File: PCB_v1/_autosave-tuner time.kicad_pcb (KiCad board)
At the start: 2 copper layers, 121 parts, among them J3 Conn_01x05_Pin, J4 Conn_01x05_Pin, J5 OLED Module Mount, SW7 SW_Push, SW8 SW_Push, U2 BQ27441-G1

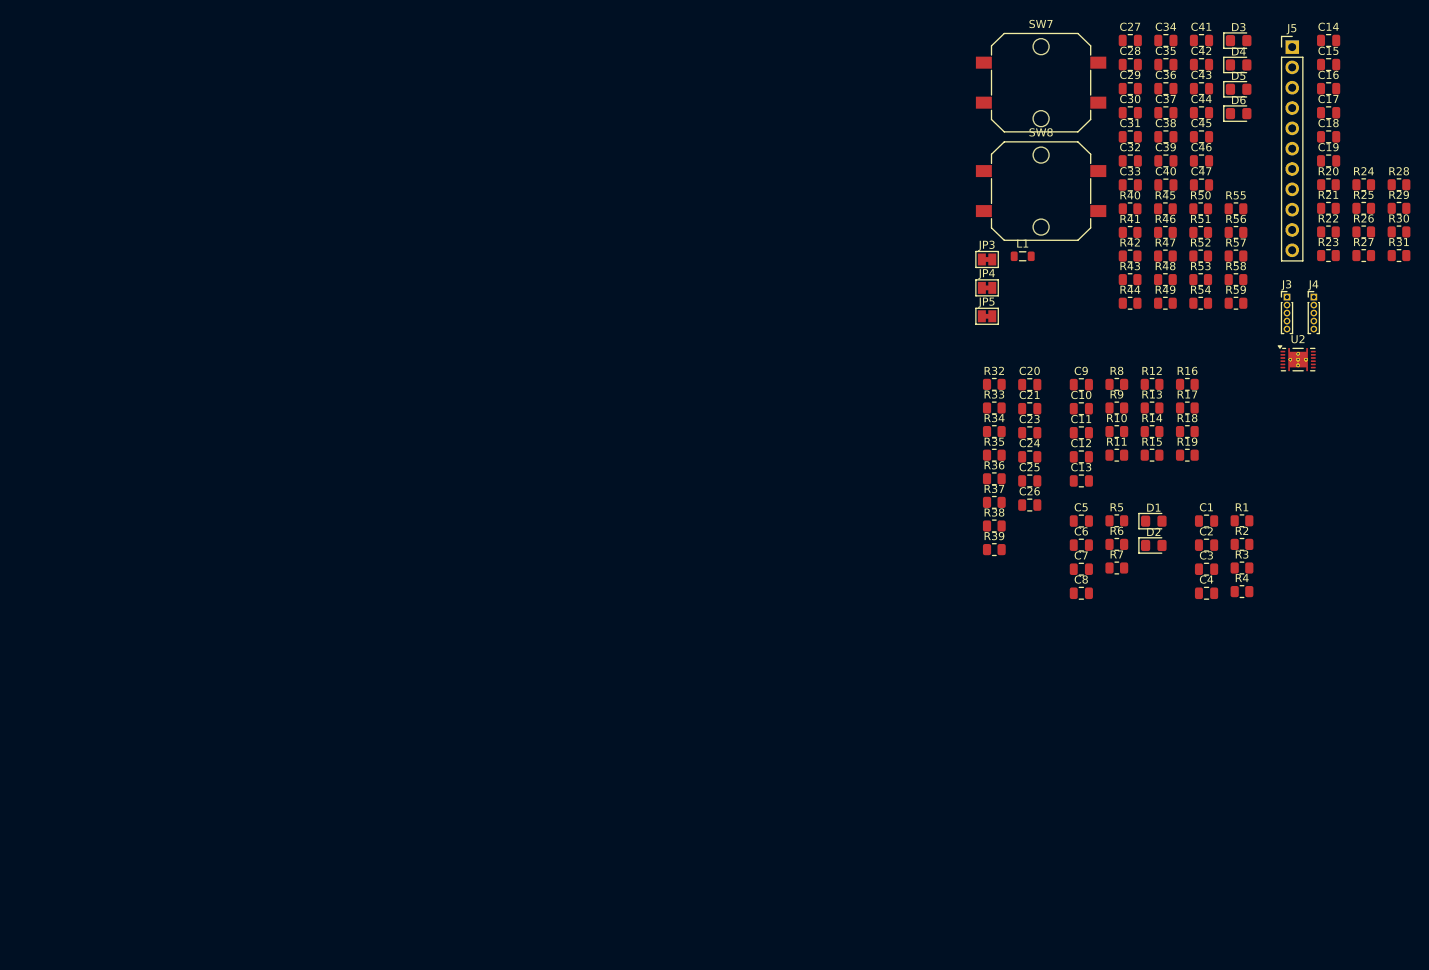
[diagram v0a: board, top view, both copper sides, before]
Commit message: adding the parts library
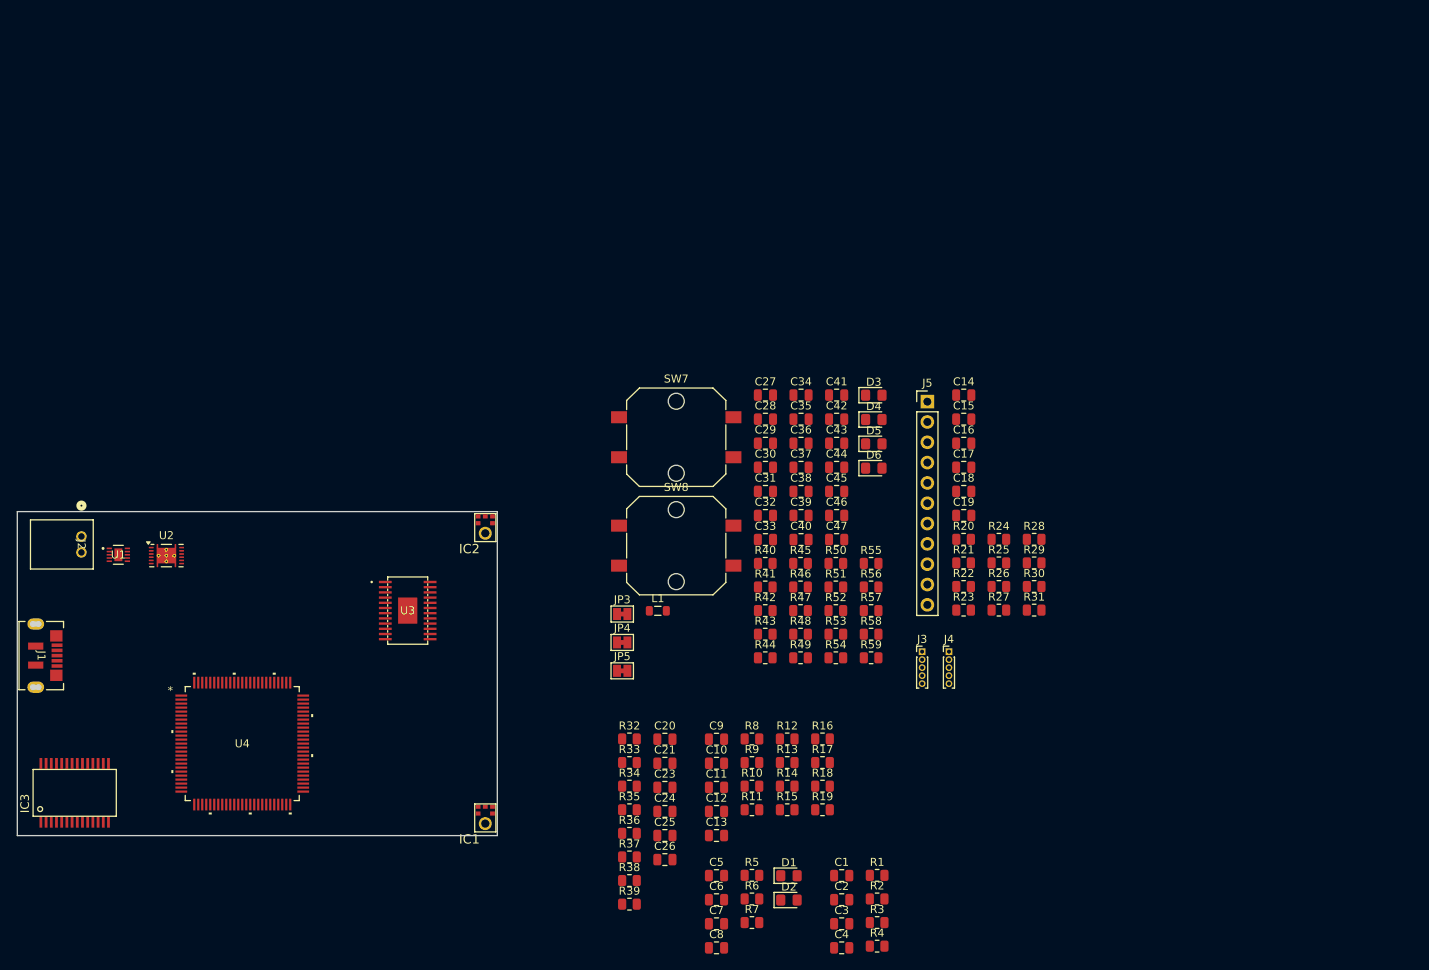
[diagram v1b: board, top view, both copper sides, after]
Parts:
- added IC1: MIC_I2S_SPH0645, Parts_Library:SPH0645LM4H, F.Cu at (153.5, 133.3)
- added IC2: MIC_I2S_SPH0645, Parts_Library:SPH0645LM4H, F.Cu at (153.5, 97.0)
- added IC3: FT2332RL, Parts_Library:SSOP28-LD, F.Cu at (102.2, 130.2)
- added J1: 1051640001, Parts_Library:CON00906_5_MOL, F.Cu at (98.0, 113.0)
- added J2: S2B-PH-K-SLFSN, Parts_Library:CONN_S2B-PH-K-S_JST, F.Cu at (103.0, 98.1)
- added U1: BQ25185DLHR, Parts_Library:WSON10_DLH_TEX, F.Cu at (107.6, 100.4)
- added U3: DRV8834PWP, Parts_Library:SOP65P640X120-25N, F.Cu at (143.8, 107.4)
- added U4: STM32F407VGT6, Parts_Library:LQFP100_14x14_STM, F.Cu at (123.1, 124.0)
- moved U2 143.6 mm to (113.6, 100.5)
- moved C14 63.6 mm to (213.3, 80.4)
- moved C15 63.6 mm to (213.3, 83.4)
- moved C16 63.6 mm to (213.3, 86.5)
- moved C17 63.6 mm to (213.3, 89.5)
- moved C18 63.6 mm to (213.3, 92.5)
- moved C19 63.6 mm to (213.3, 95.5)
- moved C20 63.6 mm to (175.9, 123.5)
- moved C21 63.6 mm to (175.9, 126.5)
- moved C23 63.6 mm to (175.9, 129.5)
- moved C24 63.6 mm to (175.9, 132.5)
- moved C25 63.6 mm to (175.9, 135.5)
- moved C26 63.6 mm to (175.9, 138.5)
- moved C41 63.6 mm to (197.4, 80.4)
- moved C42 63.6 mm to (197.4, 83.4)
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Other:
- board outline added: 60 x 40.5 mm
- copper layers 2 -> 4
